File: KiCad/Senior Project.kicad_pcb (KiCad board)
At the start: 2 copper layers, 59.2 x 89.2 mm, 49 parts, among them J1 B2B-PH-K-S, J3 Screw_Terminal_01x06, J4 Conn_ARM_JTAG_SWD_10, J5 Conn_01x03, J6 Conn_01x02, J7 USB4105-GF-A, Q2 IRLML0030, Q3 IRLML0030, Q4 IRLML0030, SW1 SW_Push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

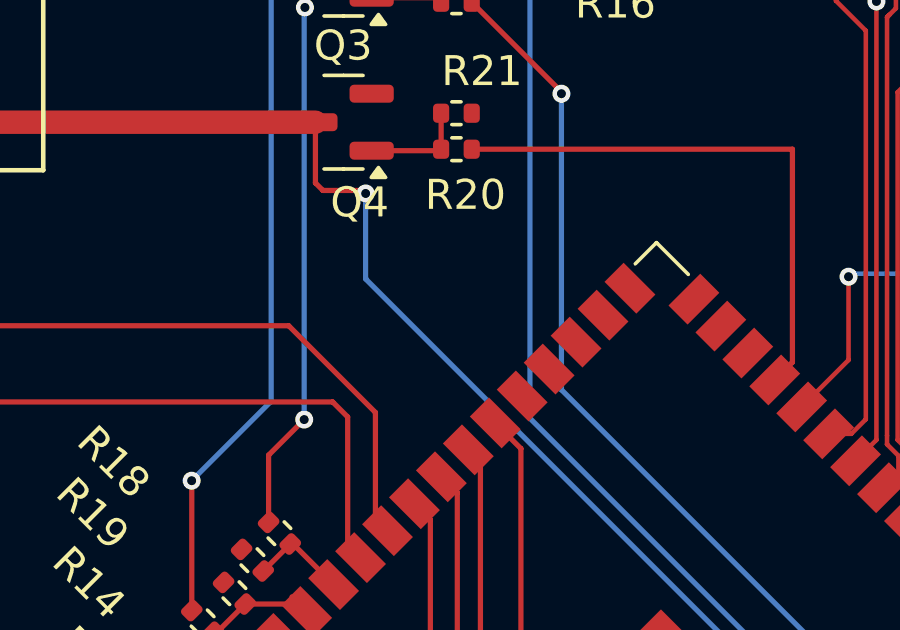
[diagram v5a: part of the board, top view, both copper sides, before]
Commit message: Switch added to PCB
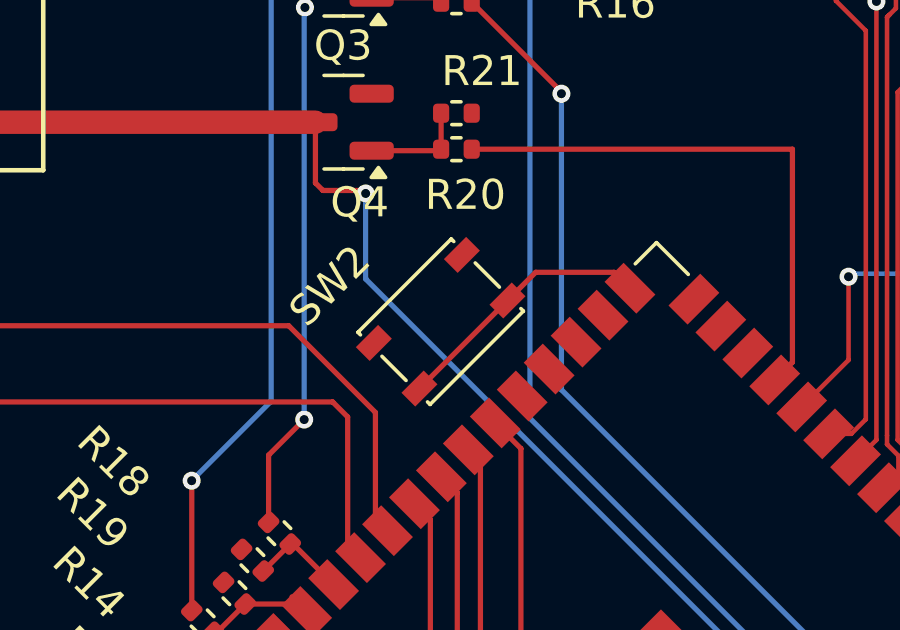
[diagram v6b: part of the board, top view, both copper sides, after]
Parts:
- added SW2: SW_Push, Button_Switch_SMD:SW_SPST_PTS810, F.Cu at (148.3, 84.8)
- J1: footprint footprints:CONN2_B2B-PH-K-S_JST -> JST_Connector:CONN2_B2B-PH-K-S_JST
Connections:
- U1 pad 27: unconnected-(U1-GPIO0/BOOT-Pad27) -> Net-(U1-GPIO0/BOOT)
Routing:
- net Net-(U1-GPIO0/BOOT): track 0.00 -> 8.84 mm

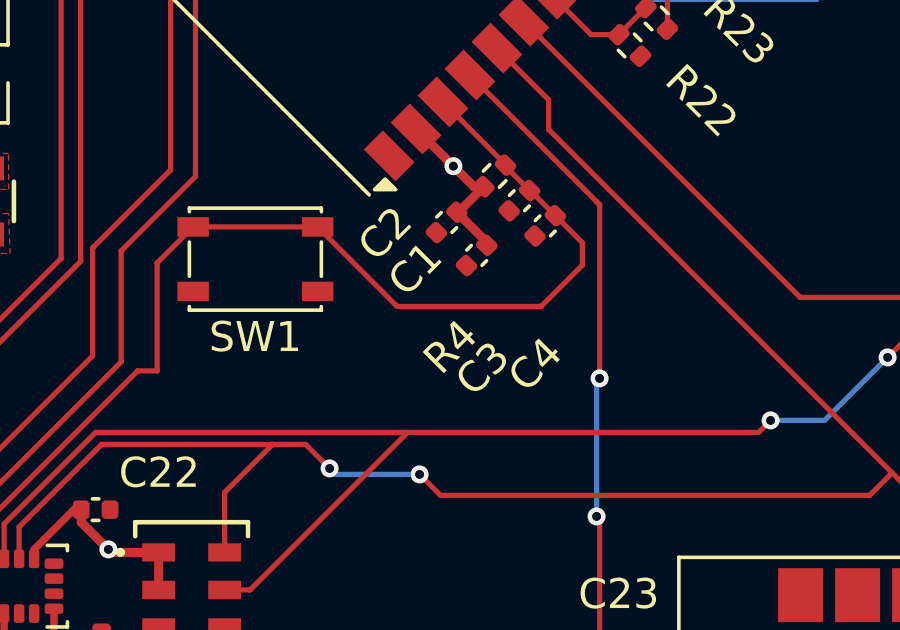
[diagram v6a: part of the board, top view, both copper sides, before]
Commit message: Final board design sent to OshPark
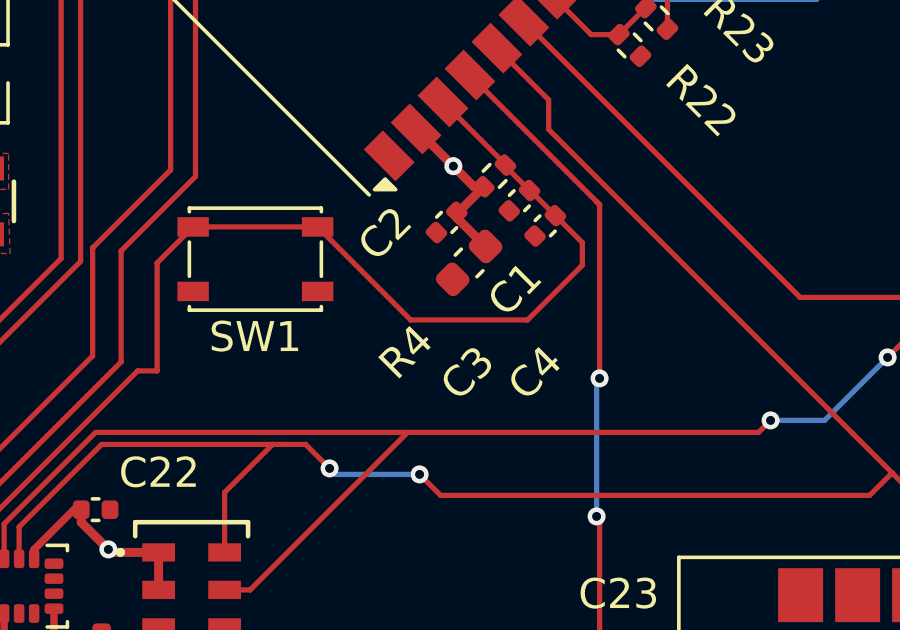
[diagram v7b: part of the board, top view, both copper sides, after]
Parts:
- C1: footprint Capacitor_SMD:C_0402_1005Metric -> Capacitor_SMD:C_0603_1608Metric
- moved C1 0.35 mm to (157.9, 111.2)
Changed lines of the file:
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@@
 		(tags "resistor")
 		(property "Reference" "R4"
-			(at -5.069383 2.991634 45)
+			(at -6.240217 2.068287 45)
 			(layer "F.SilkS")
 			(effects
@@
 		(tags "capacitor")
 		(property "Reference" "C4"
-			(at -3.504287 3.036451 45)
+			(at -3.709608 3.235014 45)
 			(layer "F.SilkS")
 			(effects
@@
 			)
 		)
-		(property "LCSC" "C14445"
+		(property "LCSC" "C52923"
 			(at 0 0 45)
 			(unlocked yes)
@@
 		)
 	)
-	(footprint "Capacitor_SMD:C_0402_1005Metric"
+	(footprint "Capacitor_SMD:C_0603_1608Metric"
 		(layer "F.Cu")
-		(at 158.2 111 -135)
-		(descr "Capacitor SMD 0402 (1005 Metric), square (rectangular) end terminal, IPC_7351 nominal, (Body size source: IPC-SM-782 page 76, https://www.pcb-3d.com/wordpress/wp-content/uploads/ipc-sm-782a_amendment_1_and_2.pdf), generated with kicad-footprint-generator")
+		(at 157.95 111.25 -135)
+		(descr "Capacitor SMD 0603 (1608 Metric), square (rectangular) end terminal, IPC_7351 nominal, (Body size source: IPC-SM-782 page 76, https://www.pcb-3d.com/wordpress/wp-content/uploads/ipc-sm-782a_amendment_1_and_2.pdf), generated with kicad-footprint-generator")
 		(tags "capacitor")
 		(property "Reference" "C1"
-			(at 1.767767 1.131371 45)
+			(at -0.459619 -1.697056 225)
 			(layer "F.SilkS")
 			(effects
@@
 		)
 		(property "Value" "22 uF"
-			(at 0 1.16 45)
+			(at 0 1.43 225)
 			(layer "F.Fab")
 			(effects
@@
 		(attr smd)
 		(fp_line
-			(start -0.107836 0.36)
-			(end 0.107836 0.36)
+			(start -0.140581 0.51)
+			(end 0.140581 0.51)
 			(stroke
 				(width 0.12)
@@
 		)
 		(fp_line
-			(start -0.107836 -0.36)
-			(end 0.107836 -0.36)
+			(start -0.140581 -0.51)
+			(end 0.140581 -0.51)
 			(stroke
 				(width 0.12)
@@
 		)
 		(fp_line
-			(start 0.91 0.46)
-			(end -0.91 0.46)
+			(start 1.48 0.73)
+			(end -1.48 0.73)
 			(stroke
 				(width 0.05)
@@
 		)
 		(fp_line
-			(start 0.91 -0.46)
-			(end 0.91 0.46)
+			(start 1.48 -0.73)
+			(end 1.48 0.73)
 			(stroke
 				(width 0.05)
@@
 		)
 		(fp_line
-			(start -0.91 0.46)
-			(end -0.91 -0.46)
+			(start -1.48 0.73)
+			(end -1.48 -0.73)
 			(stroke
 				(width 0.05)
@@
 		)
 		(fp_line
-			(start -0.91 -0.46)
-			(end 0.91 -0.46)
+			(start -1.48 -0.73)
+			(end 1.48 -0.73)
 			(stroke
 				(width 0.05)
@@
 		)
 		(fp_line
-			(start 0.5 0.25)
-			(end -0.5 0.25)
+			(start 0.8 0.4)
+			(end -0.8 0.4)
 			(stroke
 				(width 0.1)
@@
 		)
 		(fp_line
-			(start 0.5 -0.25)
-			(end 0.5 0.25)
+			(start 0.8 -0.4)
+			(end 0.8 0.4)
 			(stroke
 				(width 0.1)
@@
 		)
 		(fp_line
-			(start -0.5 0.25)
-			(end -0.5 -0.25)
+			(start -0.8 0.4)
+			(end -0.8 -0.4)
 			(stroke
 				(width 0.1)
@@
 		)
 		(fp_line
-			(start -0.5 -0.25)
-			(end 0.5 -0.25)
+			(start -0.8 -0.4)
+			(end 0.8 -0.4)
 			(stroke
 				(width 0.1)
@@
 		)
 		(fp_text user "${REFERENCE}"
-			(at 0 0 45)
+			(at 0 0 225)
 			(layer "F.Fab")
 			(effects
 				(font
-					(size 0.25 0.25)
-					(thickness 0.04)
+					(size 0.4 0.4)
+					(thickness 0.06)
 				)
 			)
 		)
 		(pad "1" smd roundrect
-			(at -0.48 0 225)
-			(size 0.56 0.62)
+			(at -0.775 0 225)
+			(size 0.9 0.95)
 			(layers "F.Cu" "F.Mask" "F.Paste")
 			(roundrect_rratio 0.25)
@@
 		)
 		(pad "2" smd roundrect
-			(at 0.48 0 225)
-			(size 0.56 0.62)
+			(at 0.775 0 225)
+			(size 0.9 0.95)
 			(layers "F.Cu" "F.Mask" "F.Paste")
 			(roundrect_rratio 0.25)
@@
 		)
 		(embedded_fonts no)
-		(model "${KICAD9_3DMODEL_DIR}/Capacitor_SMD.3dshapes/C_0402_1005Metric.wrl"
+		(model "${KICAD9_3DMODEL_DIR}/Capacitor_SMD.3dshapes/C_0603_1608Metric.wrl"
 			(offset
 				(xyz 0 0 0)
@@
 			)
 		)
-		(property "LCSC" "C1691"
+		(property "LCSC" "C15525"
 			(at 0 0 270)
 			(unlocked yes)
@@
 		(tags "capacitor")
 		(property "Reference" "C3"
-			(at -4.826004 3.093592 45)
+			(at -5.285623 2.846105 45)
 			(layer "F.SilkS")
 			(effects
@@
 	)
 	(segment
-		(start 157.860589 111.339411)
-		(end 157.860589 111.239411)
-		(width 0.2)
-		(layer "F.Cu")
-		(net 1)
-	)
-	(segment
 		(start 147.6 123.4)
 		(end 147.8413 123.4)
@@
 	)
 	(segment
-		(start 158.539411 110.560589)
-		(end 157.539411 109.560589)
-		(width 0.300387)
-		(layer "F.Cu")
-		(net 2)
-	)
-	(segment
 		(start 158.439376 108.710624)
 		(end 158.110624 108.710624)
@@
 	)
 	(segment
+		(start 157.539411 109.560589)
+		(end 157.539411 109.743395)
+		(width 0.300387)
+		(layer "F.Cu")
+		(net 2)
+	)
+	(segment
 		(start 144.41 124.505)
 		(end 144.18 124.275)
@@
 	)
 	(segment
+		(start 157.539411 109.743395)
+		(end 158.498008 110.701992)
+		(width 0.300387)
+		(layer "F.Cu")
+		(net 2)
+	)
+	(segment
 		(start 144.1125 122.775)
 		(end 144.1125 124.2075)
@@
 	)
 	(segment
+		(start 160.825 109.675)
+		(end 161.725 110.575)
+		(width 0.175)
+		(layer "F.Cu")
+		(net 46)
+	)
+	(segment
 		(start 130.8 121.14)
 		(end 140.867224 121.14)
@@
 	)
 	(segment
-		(start 159.160624 107.989376)
-		(end 159.160624 108.031802)
-		(width 0.175)
-		(layer "F.Cu")
-		(net 46)
-	)
-	(segment
-		(start 161.725 111.325)
-		(end 160.35 112.7)
+		(start 156 113.15)
+		(end 152.9 110.05)
 		(width 0.175)
 		(layer "F.Cu")
@@
 	)
 	(segment
-		(start 160.825 109.675)
-		(end 161.725 110.575)
+		(start 159.160624 107.989376)
+		(end 159.160624 108.031802)
 		(width 0.175)
 		(layer "F.Cu")
@@
 	)
 	(segment
-		(start 160.35 112.7)
-		(end 155.55 112.7)
+		(start 159.9 113.15)
+		(end 156 113.15)
 		(width 0.175)
 		(layer "F.Cu")
@@
 	)
 	(segment
-		(start 155.55 112.7)
-		(end 152.9 110.05)
+		(start 161.725 111.325)
+		(end 159.9 113.15)
 		(width 0.175)
 		(layer "F.Cu")

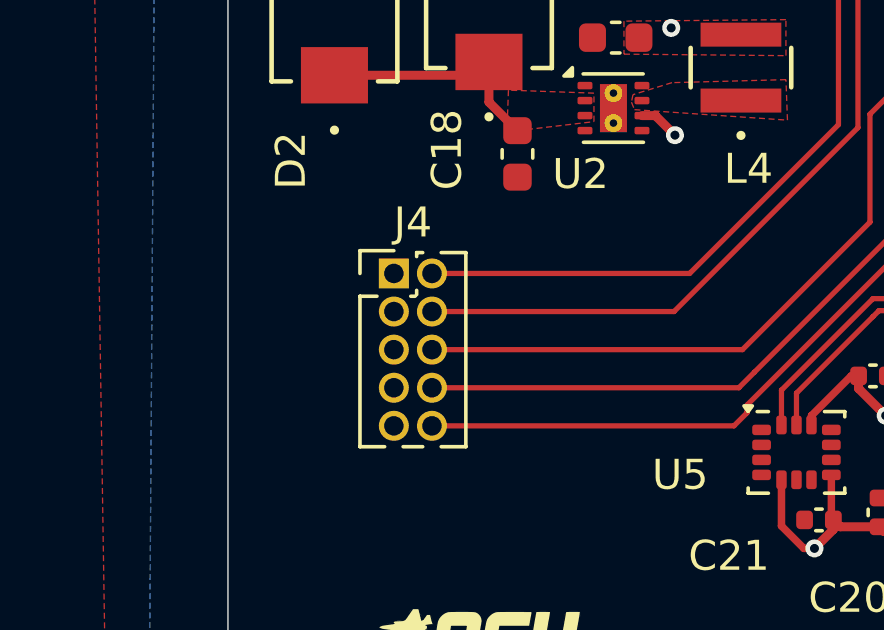
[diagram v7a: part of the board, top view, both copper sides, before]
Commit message: Working radio, imu, and barometer code
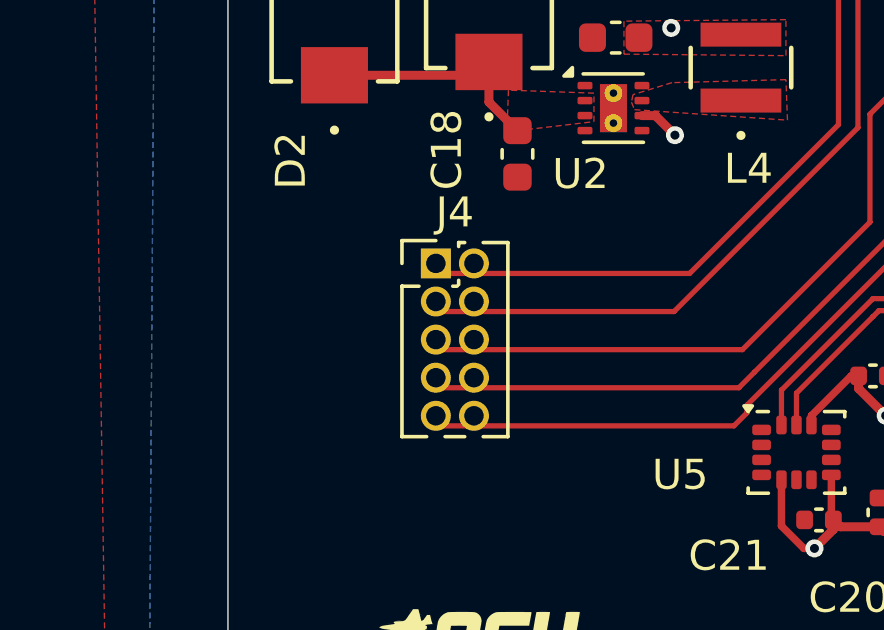
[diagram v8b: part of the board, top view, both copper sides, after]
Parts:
- moved J4 1.44 mm to (130.9, 115.7)
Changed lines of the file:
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@@
 	(footprint "Connector_PinHeader_1.27mm:PinHeader_2x05_P1.27mm_Vertical"
 		(layer "F.Cu")
-		(at 129.53 116.06)
+		(at 130.93 115.725)
 		(descr "Through hole straight pin header, 2x05, 1.27mm pitch, double rows")
 		(tags "Through hole pin header THT 2x05 1.27mm double row")
